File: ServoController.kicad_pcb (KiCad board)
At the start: 2 copper layers, 42 x 77 mm, 76 parts, among them J1 Conn_01x06_Male, J10 ServoInputSW, J11 ServoOut, J12 ServoInputSW, J13 ServoOut, J14 ServoInputSW, J15 ServoOut, J16 ServoInputSW, J17 ServoOut, J18 ServoInputSW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

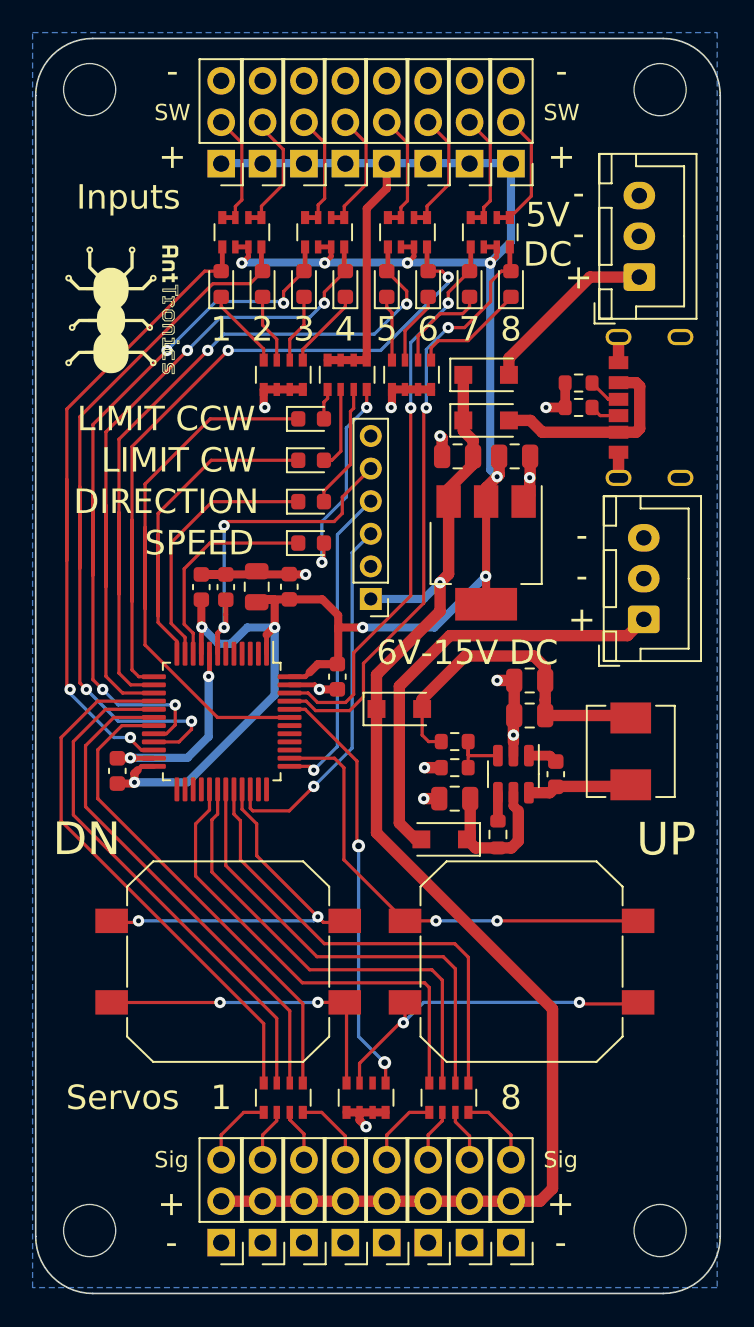
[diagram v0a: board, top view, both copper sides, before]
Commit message: Silkscreen updates
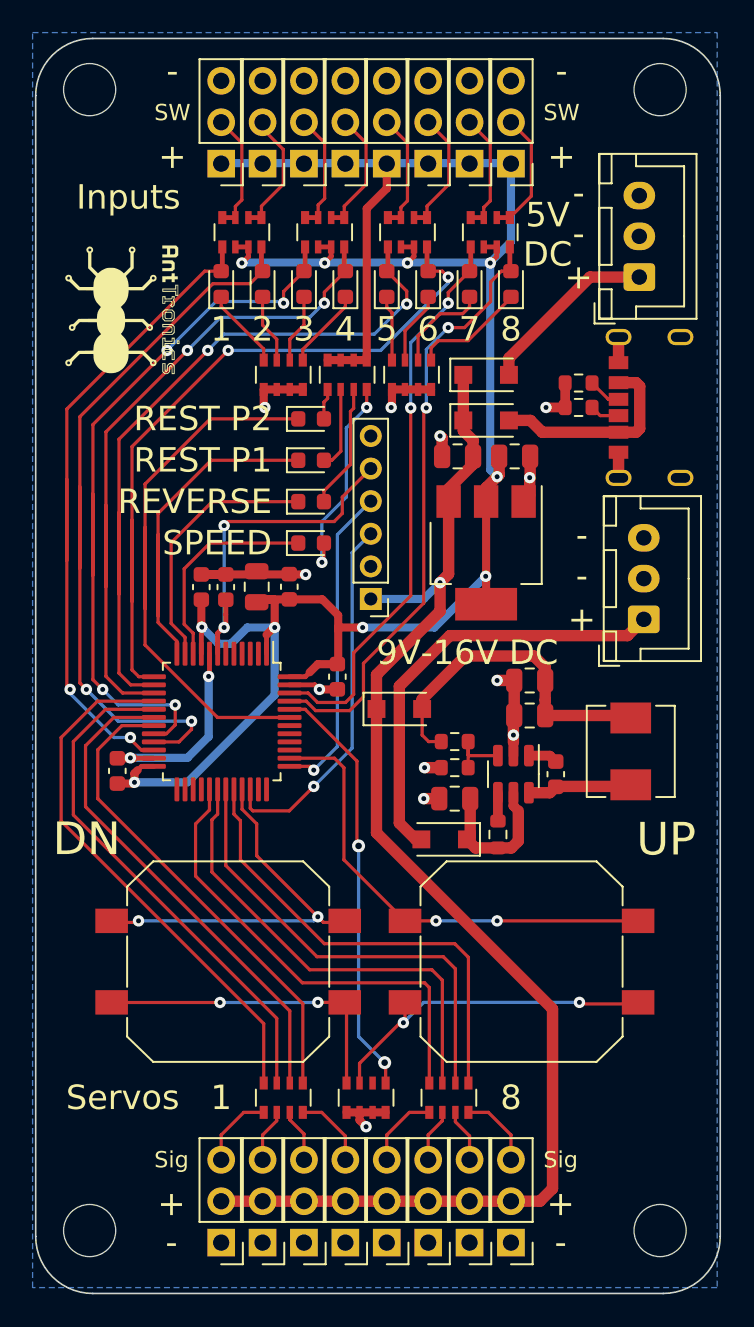
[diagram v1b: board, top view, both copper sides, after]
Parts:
- renumbered C11 to C12, C12 to C13
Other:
- board text added: "9V-16V DC"
- board text added: "REST P1"
- board text added: "REST P2"
- board text added: "REVERSE"
- board text removed: "6V-15V DC"
- board text removed: "DIRECTION"
- board text removed: "LIMIT CCW"
- board text removed: "LIMIT CW"
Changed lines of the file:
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@@
     (pad_to_mask_clearance 0)
     (pcbplotparams
-      (layerselection 0x00010fc_ffffffff)
+      (layerselection 0x00200a0_7ffffffe)
       (disableapertmacros false)
       (usegerberextensions false)
@@
       (svguseinch false)
       (svgprecision 6)
-      (excludeedgelayer true)
+      (excludeedgelayer false)
       (plotframeref false)
       (viasonmask false)
@@
       (sketchpadsonfab false)
       (subtractmaskfromsilk false)
-      (outputformat 1)
+      (outputformat 5)
       (mirror false)
-      (drillshape 1)
+      (drillshape 2)
       (scaleselection 1)
-      (outputdirectory "")
+      (outputdirectory "plots/")
     )
   )
@@
     (property "Sheetname" "")
     (attr smd)
-    (fp_text reference "C11" (at 0 -1.68) (layer "F.Fab") hide
+    (fp_text reference "C12" (at 0 -1.68) (layer "F.Fab") hide
       (effects (font (size 1 1) (thickness 0.15)))
     )
@@
     (fp_line (start 7.45 3.4) (end 7.45 -2.35) (layer "F.Fab") (width 0.1))
     (fp_line (start 0 -1.35) (end 0.625 -2.35) (layer "F.Fab") (width 0.1))
-    (pad "1" thru_hole roundrect (at 0 0 90) (size 1.7 1.95) (drill 0.95) (layers *.Cu *.Mask) (roundrect_rratio 0.147059)
+    (pad "1" thru_hole roundrect (at 0 0 90) (size 1.7 1.95) (drill 0.95) (layers *.Cu *.Mask) (roundrect_rratio 0.1470588235)
       (net 75 "Net-(D7-Pad2)") (pinfunction "Pin_1") (pintype "passive"))
     (pad "2" thru_hole oval (at 2.5 0 90) (size 1.7 1.95) (drill 0.95) (layers *.Cu *.Mask)
@@
     (fp_line (start -2.45 3.4) (end 7.45 3.4) (layer "F.Fab") (width 0.1))
     (fp_line (start 7.45 3.4) (end 7.45 -2.35) (layer "F.Fab") (width 0.1))
-    (pad "1" thru_hole roundrect (at 0 0 90) (size 1.7 1.95) (drill 0.95) (layers *.Cu *.Mask) (roundrect_rratio 0.147059)
+    (pad "1" thru_hole roundrect (at 0 0 90) (size 1.7 1.95) (drill 0.95) (layers *.Cu *.Mask) (roundrect_rratio 0.1470588235)
       (net 28 "Net-(D1-Pad2)") (pinfunction "Pin_1") (pintype "passive"))
     (pad "2" thru_hole oval (at 2.5 0 90) (size 1.7 1.95) (drill 0.95) (layers *.Cu *.Mask)
@@
     (property "Sheetname" "")
     (attr smd)
-    (fp_text reference "C12" (at 0 -1.68) (layer "F.Fab") hide
+    (fp_text reference "C13" (at 0 -1.68) (layer "F.Fab") hide
       (effects (font (size 1 1) (thickness 0.15)))
     )
@@
     (effects (font (size 1.5 1.5) (thickness 0.2)))
   )
-  (gr_text "DIRECTION" (at 179.5075 73.92) (layer "F.SilkS")
-    (effects (font (size 1.5 1.5) (thickness 0.2)))
+  (gr_text "REVERSE" (at 186 73.92) (layer "F.SilkS")
+    (effects (font (size 1.5 1.5) (thickness 0.2)) (justify right))
   )
   (gr_text "-" (at 179.886 47.766 180) (layer "F.SilkS")
@@
     (effects (font (size 1.5 1.5) (thickness 0.3)))
   )
-  (gr_text "SPEED" (at 181.5395 76.46) (layer "F.SilkS")
-    (effects (font (size 1.5 1.5) (thickness 0.2)))
+  (gr_text "SPEED" (at 186 76.46) (layer "F.SilkS")
+    (effects (font (size 1.5 1.5) (thickness 0.2)) (justify right))
   )
   (gr_text "Inputs" (at 173.99 55.245) (layer "F.SilkS")
     (effects (font (size 1.5 1.5) (thickness 0.2)) (justify left))
   )
-  (gr_text "LIMIT CCW" (at 179.5075 68.84) (layer "F.SilkS")
-    (effects (font (size 1.5 1.5) (thickness 0.2)))
+  (gr_text "REST P2" (at 186 68.84) (layer "F.SilkS")
+    (effects (font (size 1.5 1.5) (thickness 0.2)) (justify right))
   )
   (gr_text "5" (at 193.04 63.34) (layer "F.SilkS")
@@
     (effects (font (size 1.5 1.5) (thickness 0.3)))
   )
-  (gr_text "6V-15V DC" (at 192.405 83.185) (layer "F.SilkS")
+  (gr_text "9V-16V DC" (at 192.405 83.185) (layer "F.SilkS")
     (effects (font (size 1.5 1.5) (thickness 0.2)) (justify left))
   )
@@
     (effects (font (size 1.5 1.5) (thickness 0.3)))
   )
-  (gr_text "LIMIT CW" (at 180.2695 71.38) (layer "F.SilkS")
-    (effects (font (size 1.5 1.5) (thickness 0.2)))
+  (gr_text "REST P1" (at 186 71.38) (layer "F.SilkS")
+    (effects (font (size 1.5 1.5) (thickness 0.2)) (justify right))
   )
   (gr_text "+" (at 203.708 117.094 180) (layer "F.SilkS")
